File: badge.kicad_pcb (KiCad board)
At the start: 2 copper layers, 99.1 x 99.1 mm, 33 parts, among them J1 DevKitC_L, J10 HT024SQV003NH, J2 DevKitC_R, J4 EXT1_1, J5 EXT1_2, J6 EXT1_3, J7 EXT2_1, J8 EXT2_2, J9 EXT2_3, SW1 UP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

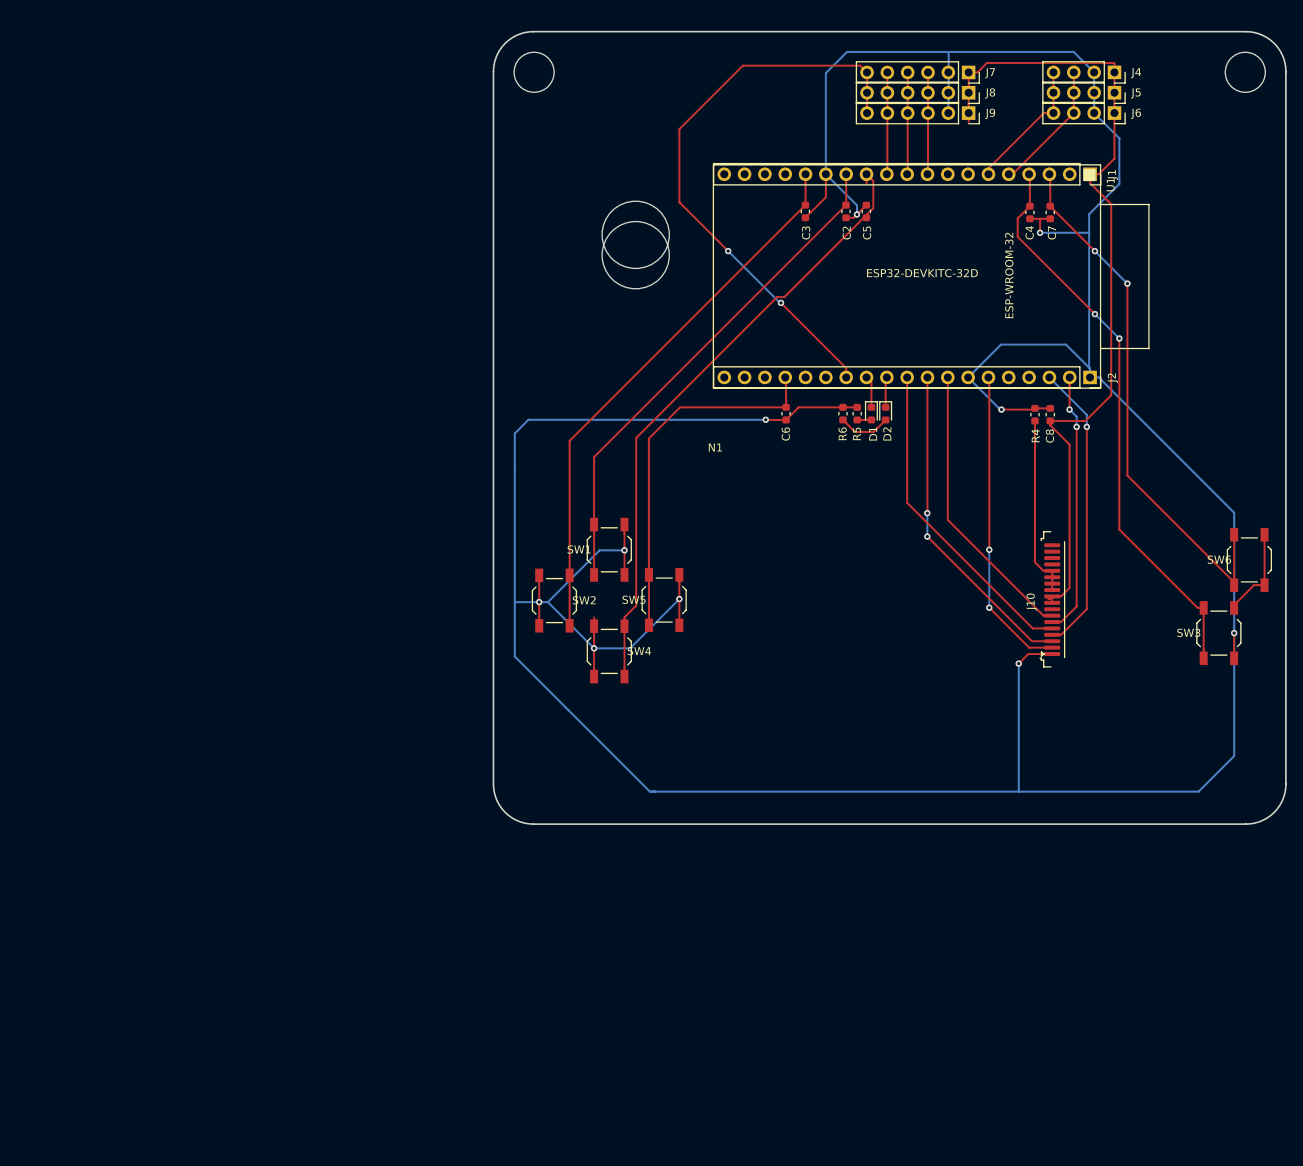
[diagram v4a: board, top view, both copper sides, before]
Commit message: v0.2 add dust sensor and 5 way tact switch
* LED direction corrected
* Pin adjusted
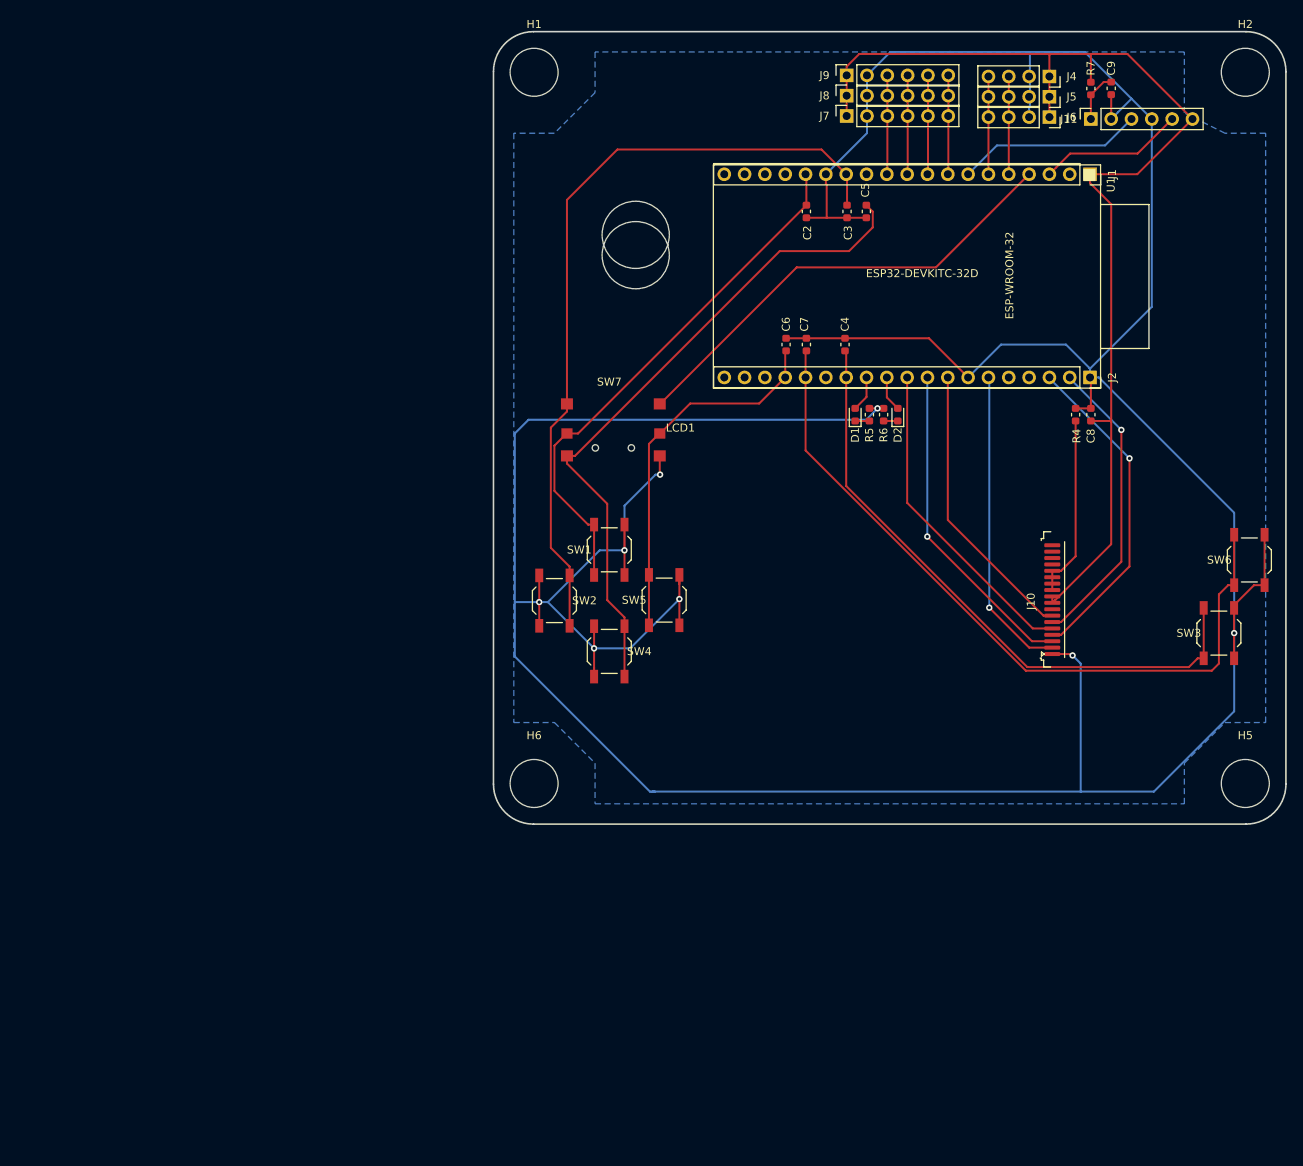
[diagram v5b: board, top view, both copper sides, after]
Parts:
- removed N1: 2.4" LCD, custom_footprint:2.4INCH_TFT_LCD_18P_0.80mm_FOLD
- added C9: 0603/220uF/16V, Capacitor_SMD:C_0603_1608Metric, F.Cu at (178.8, 19.8)
- added H5: MountingHole, custom_footprint:LanyardHole_6mm, F.Cu at (195.6, 106.7)
- added H6: MountingHole, custom_footprint:LanyardHole_6mm, F.Cu at (106.7, 106.7)
- added J11: EXT3, custom_footprint:PinSocket_1x06_P2.54mm_Vertical_NO3D, F.Cu at (176.3, 23.6)
- added LCD1: 2.4" LCD, custom_footprint:2.4INCH_TFT_LCD_18P_0.80mm_FOLD, F.Cu at (127.3, 63.0)
- added R7: 0603/220R, Resistor_SMD:R_0603_1608Metric, F.Cu at (176.3, 19.8)
- added SW7: SW_DIP_x03, custom_footprint:ITS-1500S, F.Cu at (116.6, 62.5)
- H1, H2: footprint MountingHole:MountingHole_5mm -> custom_footprint:LanyardHole_6mm
- moved C7 34.7 mm to (140.7, 51.8), turned to 270 degrees
- moved C4 28.4 mm to (145.5, 51.8), turned to 270 degrees
- moved J7 16.2 mm to (145.8, 23.2), turned to 90 degrees
- moved J9 16.0 mm to (145.8, 18.2), turned to 90 degrees
- moved J8 15.3 mm to (145.8, 20.7), turned to 90 degrees
- moved C6 8.64 mm to (138.2, 51.8), turned to 270 degrees
- moved J4 8.15 mm to (171.1, 18.3)
- moved J5 8.15 mm to (171.1, 20.8)
- moved J6 8.15 mm to (171.1, 23.4)
- moved C3 5.21 mm to (145.8, 35.2)
- moved R6 5.08 mm to (150.4, 60.6)
- moved C8 5.08 mm to (176.3, 60.6)
- moved R4 5.08 mm to (174.4, 60.6)
- moved C2 4.95 mm to (140.7, 35.2)
- moved D1 2.04 mm to (146.8, 60.6), turned to 90 degrees
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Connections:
- C2 pad 2: /GPIO12 -> /GPIO13
- C3 pad 2: /GPIO13 -> /GPIO12
- C4 pad 2: /GPIO39 -> /GPIO4
- C7 pad 2: /GPIO36 -> /GPIO2
- D1 pad 1: /GPIO16 -> Net-(D1-Pad1)
- D1 pad 2: Net-(D1-Pad2) -> /GPIO16
- D2 pad 1: /GPIO17 -> Net-(D2-Pad1)
- D2 pad 2: Net-(D2-Pad2) -> /GPIO17
- J1 pad 8: Net-(J1-Pad8) -> /GPIO33
- J2 pad 15: Net-(J2-Pad15) -> /GPIO2
- J7 pad 3: /GPIO25 -> /GPIO27
- J7 pad 5: /GPIO27 -> /GPIO25
- J7 pad 6: /GPIO4 -> /GPIO33
- J8 pad 3: /GPIO25 -> /GPIO27
- J8 pad 5: /GPIO27 -> /GPIO25
- J8 pad 6: /GPIO4 -> /GPIO33
- J9 pad 3: /GPIO25 -> /GPIO27
- J9 pad 5: /GPIO27 -> /GPIO25
- J9 pad 6: /GPIO4 -> /GPIO33
- R5 pad 2: Net-(D1-Pad2) -> Net-(D1-Pad1)
- R6 pad 2: Net-(D2-Pad2) -> Net-(D2-Pad1)
- SW1 pad 1: /GPIO12 -> /GPIO13
- SW2 pad 1: /GPIO13 -> /GPIO12
- SW3 pad 1: /GPIO39 -> /GPIO4
- SW6 pad 1: /GPIO36 -> /GPIO2
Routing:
- net /GPIO2: track 0.00 -> 93.3 mm
- net /GPIO36: track 67.2 -> 18.2 mm, vias 2 -> 0
- net +3V3: track 104.3 -> 142.1 mm
- net /GPIO12: track 63.1 -> 97.7 mm
- net GND: track 484.2 -> 512.3 mm, vias 10 -> 8
- net /GPIO32: track 0.00 -> 23.3 mm
- net /GPIO39: track 71.3 -> 58.1 mm, vias 2 -> 0
- net /GPIO33: track 0.00 -> 12.8 mm
- net Net-(D2-Pad2): track 6.58 -> 0.00 mm
- net /GPIO14: track 77.8 -> 84.1 mm
- net Net-(C9-Pad1): track 0.00 -> 6.23 mm
- net /GPIO4: track 71.9 -> 77.8 mm, vias 2 -> 0
- net /LCD_DC: track 36.8 -> 41.0 mm
- net /GPIO34: track 16.4 -> 12.2 mm
- net /GPIO35: track 16.0 -> 12.2 mm
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- added copper zone on B.Cu, net GND

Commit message: v0.3 0.3mm track, SMT/THT pinsocket support
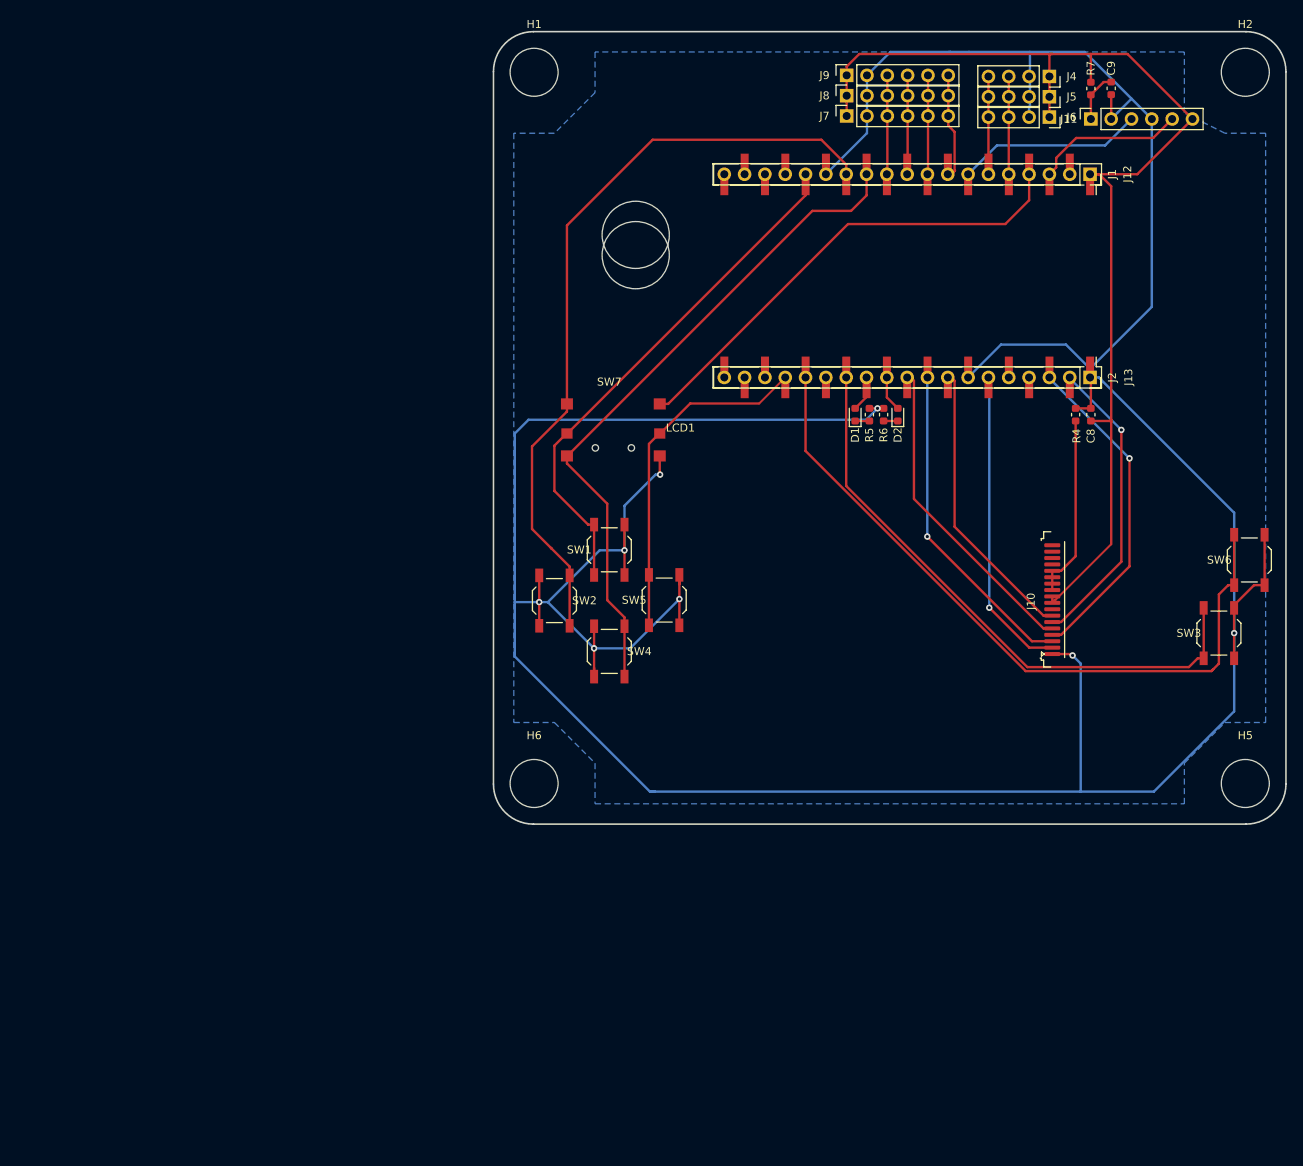
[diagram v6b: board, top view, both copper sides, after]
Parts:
- removed C2, C3, C4, C5, C6, C7: 0.1uF, Capacitor_SMD:C_0603_1608Metric
- removed U1: ESP32-DEVKITC-32D, custom_footprint:MODULE_ESP32-DEVKITC-32D-SILKONLY
- added J12: DevKitC_L_SMD, Connector_PinSocket_2.54mm:PinSocket_1x19_P2.54mm_Vertical_SMD_Pin1Right, F.Cu at (153.3, 30.5)
- added J13: DevKitC_R_SMD, Connector_PinSocket_2.54mm:PinSocket_1x19_P2.54mm_Vertical_SMD_Pin1Left, F.Cu at (153.3, 55.9)
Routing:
- net GND: track 512.3 -> 479.8 mm
- net /GPIO39: track 58.1 -> 63.3 mm
- net /GPIO33: track 12.8 -> 15.7 mm
- net /GPIO36: track 18.2 -> 20.6 mm
- net +3V3: track 142.1 -> 144.4 mm
- net /GPIO14: track 84.1 -> 86.1 mm
- net /VSPI_MISO: track 35.8 -> 37.7 mm
- net /GPIO34: track 12.2 -> 13.9 mm
- net +5V: track 0.00 -> 1.68 mm
- net /GPIO32: track 23.3 -> 25.0 mm
- net /GPIO27: track 12.8 -> 14.4 mm
- net /GPIO25: track 12.8 -> 14.4 mm
- net /VSPI_SCK: track 40.9 -> 42.6 mm
- net /GPIO17: track 4.44 -> 6.09 mm
- net /LCD_DC: track 41.0 -> 42.6 mm
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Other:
- net class Default: trace_width 0.25 -> 0.3

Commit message: Vertical badge style
* Change C9 footprint to 2816
* Add 3D model for 5 wat tactile switch
* 3D models should be located in ${HOME}/kicad/template
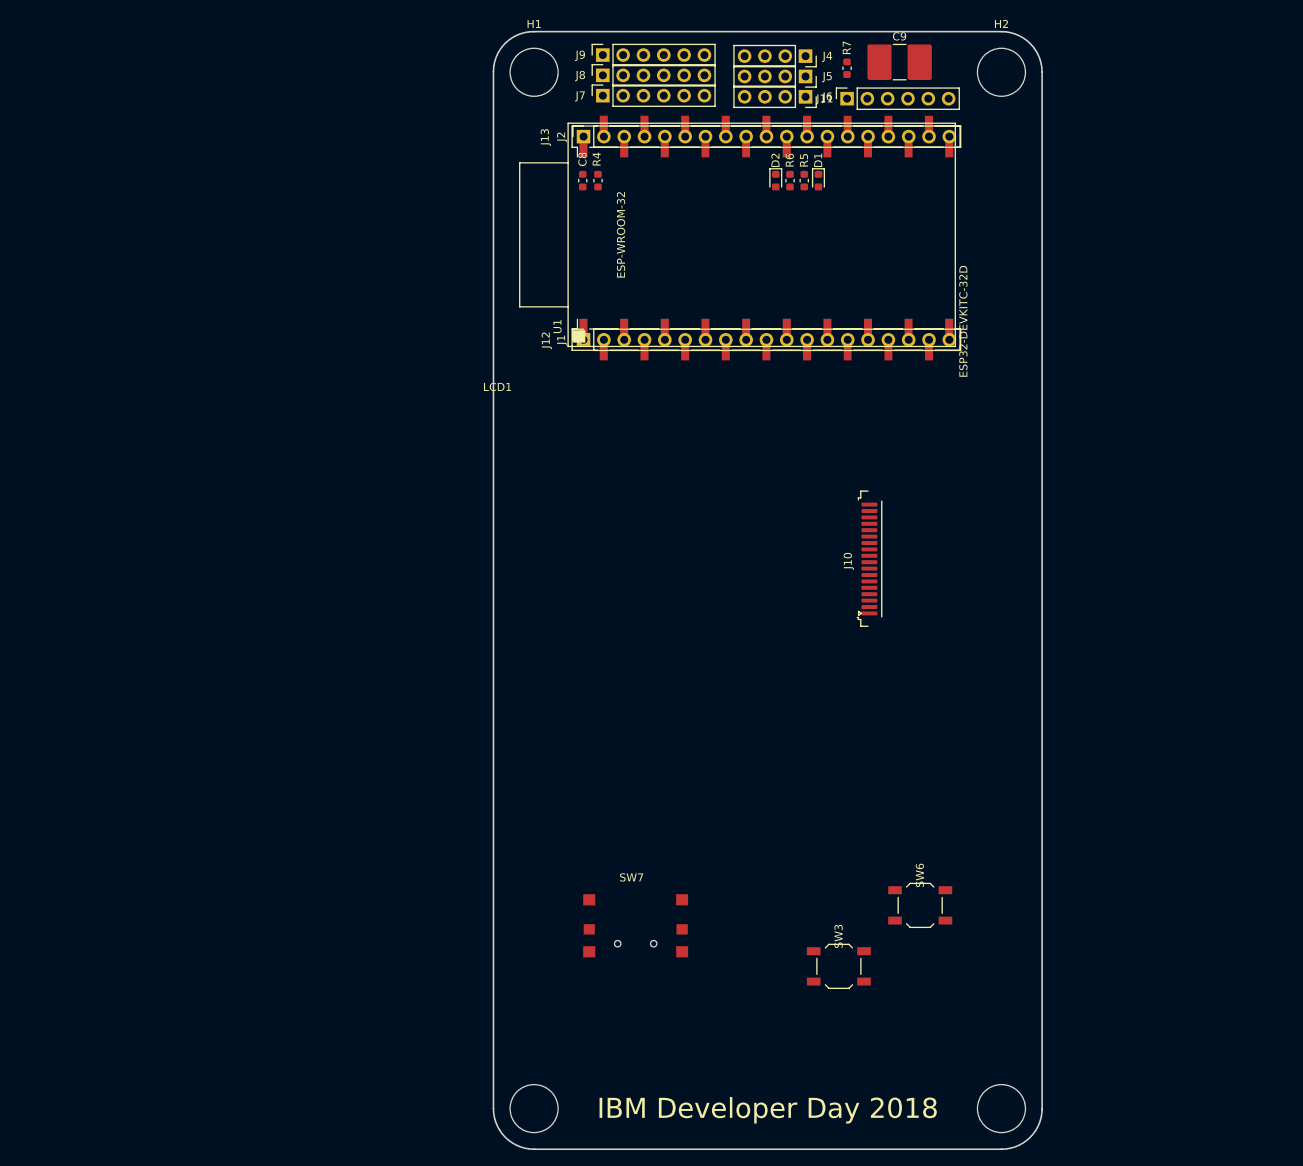
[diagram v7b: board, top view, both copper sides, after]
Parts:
- removed H3, H4: MountingHole, MountingHole:MountingHole_8.4mm_M8
- removed SW1: UP, Button_Switch_SMD:SW_SPST_TL3342
- removed SW2: LEFT, Button_Switch_SMD:SW_SPST_TL3342
- removed SW4: DOWN, Button_Switch_SMD:SW_SPST_TL3342
- removed SW5: RIGHT, Button_Switch_SMD:SW_SPST_TL3342
- added U1: ESP32-DEVKITC-32D, custom_footprint:MODULE_ESP32-DEVKITC-32D-SILKONLY, F.Cu at (132.1, 38.1)
- C9: value 0603/220uF/16V -> 2917/220uF/16V; footprint Capacitor_SMD:C_0603_1608Metric -> Capacitor_SMD:C_2816_7142Metric
- SW7: footprint custom_footprint:ITS-1500S -> custom_footprint:ITS-1500S-A
- moved J2 70.1 mm to (112.9, 25.8), turned to 90 degrees
- moved C8 69.9 mm to (112.8, 31.3), turned to 270 degrees
- moved J1 66.6 mm to (112.9, 51.2), turned to 90 degrees
- moved R4 66.5 mm to (114.7, 31.3), turned to 270 degrees
- moved SW3 63.2 mm to (144.8, 129.5), turned to 0 degrees
- moved SW7 62.0 mm to (119.4, 124.5)
- moved SW6 59.6 mm to (154.9, 121.9), turned to 0 degrees
- moved H5 50.8 mm to (165.1, 147.3)
- moved H6 40.6 mm to (106.7, 147.3)
- moved J13 34.9 mm to (135.7, 25.8), turned to 90 degrees
- moved D2 33.0 mm to (136.9, 31.3), turned to 270 degrees
- moved R6 31.5 mm to (138.7, 31.3), turned to 90 degrees
- moved J11 30.6 mm to (145.8, 21.1)
- moved R7 30.6 mm to (145.8, 17.3)
- moved J7 30.6 mm to (115.3, 20.7)
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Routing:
- net GND: track 479.8 -> 0.00 mm, vias 8 -> 0
- net +3V3: track 144.4 -> 0.00 mm
- net /GPIO12: track 97.4 -> 0.00 mm
- net /GPIO2: track 92.3 -> 0.00 mm
- net /GPIO14: track 86.1 -> 0.00 mm
- net /GPIO4: track 76.5 -> 0.00 mm
- net /GPIO13: track 65.6 -> 0.00 mm
- net /GPIO39: track 63.3 -> 0.00 mm
- net /GPIO15: track 45.1 -> 0.00 mm
- net /LCD_DC: track 42.6 -> 0.00 mm, vias 1 -> 0
- net /VSPI_SCK: track 42.6 -> 0.00 mm, vias 1 -> 0
- net /VSPI_CS: track 41.4 -> 0.00 mm
- net /LCD_RST: track 40.6 -> 0.00 mm, vias 1 -> 0
- net /VSPI_MOSI: track 39.1 -> 0.00 mm, vias 1 -> 0
- net /VSPI_MISO: track 37.7 -> 0.00 mm
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- removed copper zone on B.Cu, net GND
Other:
- board size 99.1 x 99.1 mm -> 68.6 x 139.7 mm
- board text added: "IBM Developer Day 2018"
